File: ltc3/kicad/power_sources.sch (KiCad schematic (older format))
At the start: 8 parts

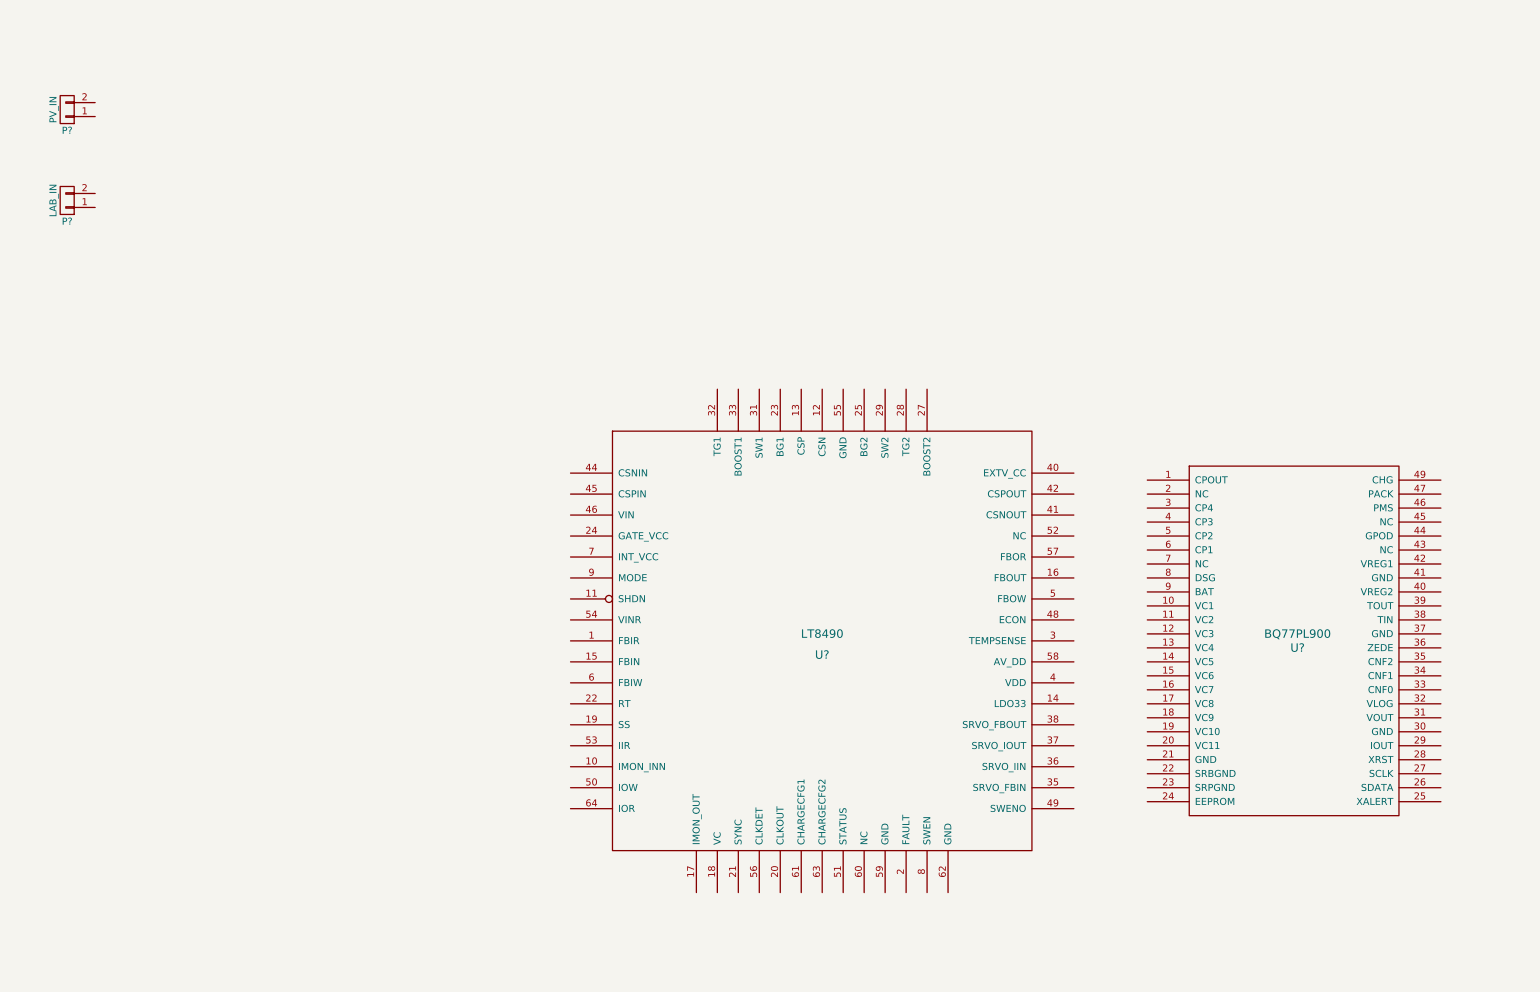
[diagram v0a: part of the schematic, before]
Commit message: Progress on merging master with Charging_Circuit branch.
Still have plenty of schematic clean-up to perform.  There's a lot
going on around the LT8490.
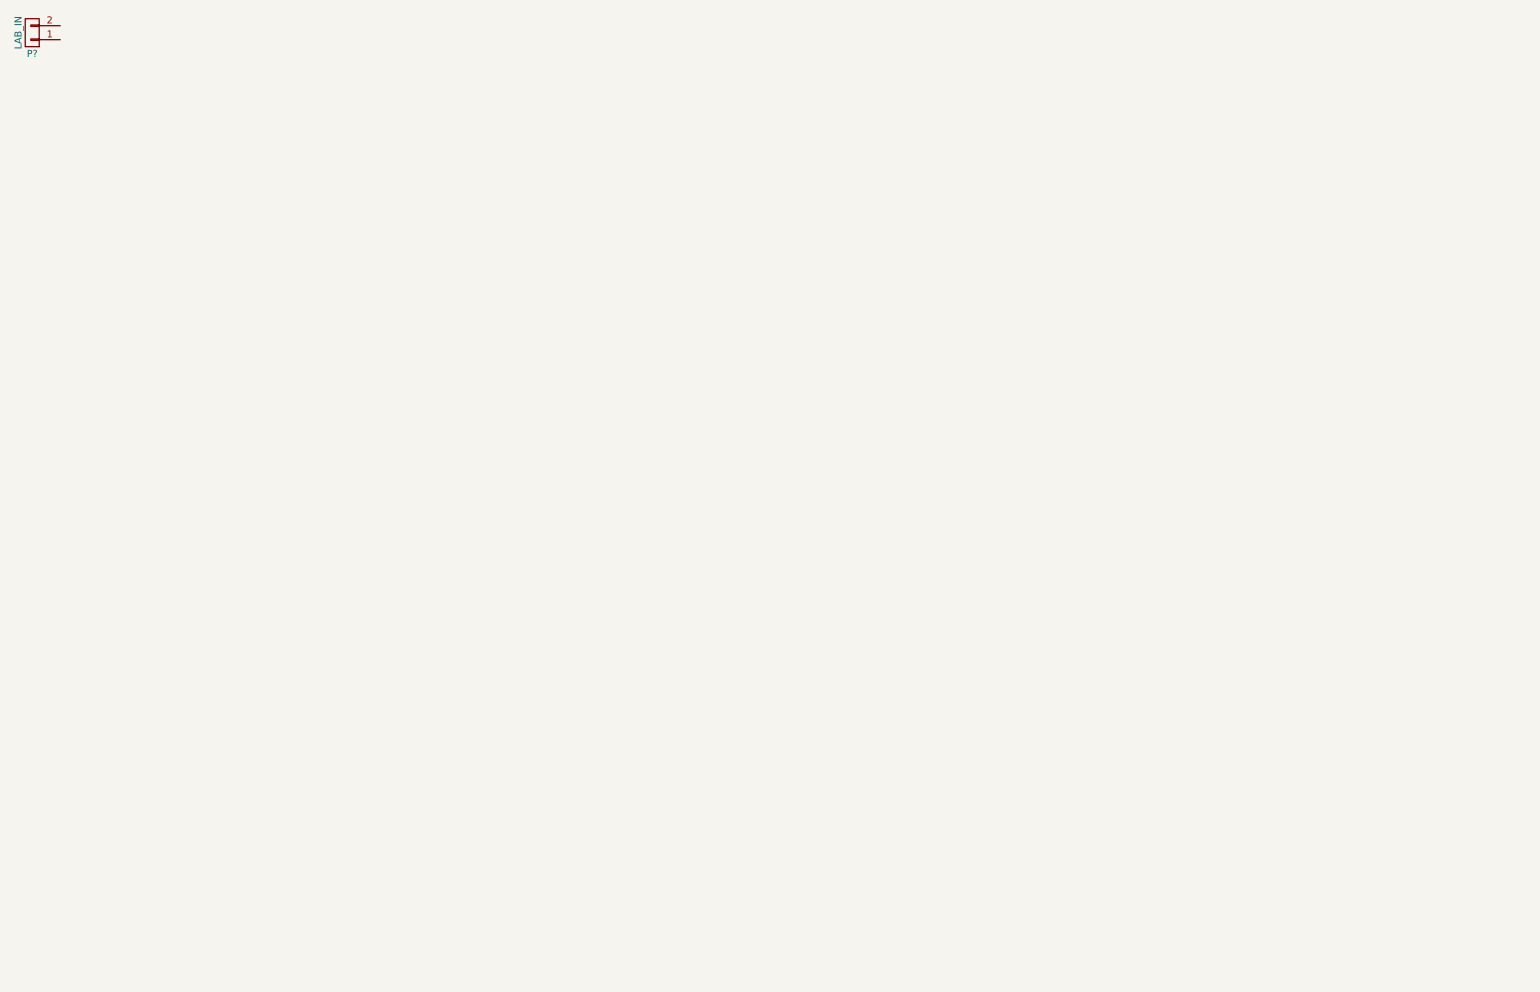
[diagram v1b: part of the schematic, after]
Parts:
- removed P?: PV_IN, symbol CONN_01X02
- removed U?: BQ77PL900, symbol BQ77PL900
- removed U?: LT8490, symbol LT8490
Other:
- moved on the sheet: P?
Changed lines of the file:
@@
-$Comp
-L CONN_01X02 P?
-U 1 1 5583855E
-P 1100 1300
-F 0 "P?" H 1100 1450 50  0000 C CNN
-F 1 "PV_IN" V 1200 1300 50  0000 C CNN
-F 2 "" H 1100 1300 60  0000 C CNN
-F 3 "" H 1100 1300 60  0000 C CNN
-	1    1100 1300
-	-1   0    0    1
-$EndComp
 $Comp
 L CONN_01X02 P?
 U 1 1 55838585
-P 1100 1950
-F 0 "P?" H 1100 2100 50  0000 C CNN
-F 1 "LAB_IN" V 1200 1950 50  0000 C CNN
-F 2 "" H 1100 1950 60  0000 C CNN
-F 3 "" H 1100 1950 60  0000 C CNN
-	1    1100 1950
+P 850 750
+F 0 "P?" H 850 900 50  0000 C CNN
+F 1 "LAB_IN" V 950 750 50  0000 C CNN
+F 2 "" H 850 750 60  0000 C CNN
+F 3 "" H 850 750 60  0000 C CNN
+	1    850  750
 	-1   0    0    1
 $EndComp
@@
 Text Notes 15850 8850 2    60   ~ 0
 Temperature Sensor, Main Battery
-$Comp
-L LT8490 U?
-U 1 1 560CC4C9
-P 6500 5100
-F 0 "U?" H 6500 5000 60  0000 C CNN
-F 1 "LT8490" H 6500 5150 60  0000 C CNN
-F 2 "" H 6550 5200 60  0000 C CNN
-F 3 "" H 6550 5200 60  0000 C CNN
-	1    6500 5100
-	1    0    0    -1
-$EndComp
-$Comp
-L BQ77PL900 U?
-U 1 1 560CC0A7
-P 9900 5100
-F 0 "U?" H 9900 5050 60  0000 C CNN
-F 1 "BQ77PL900" H 9900 5150 60  0000 C CNN
-F 2 "" H 9900 5100 60  0000 C CNN
-F 3 "" H 9900 5100 60  0000 C CNN
-	1    9900 5100
-	1    0    0    -1
-$EndComp
 $EndSCHEMATC

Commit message: Deleted "Power Sources" sheet.
Moved what little circuity it contained into the "Battery Charging"
and "Battery Balancing" sheets.
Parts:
- removed C?: 470p, symbol C
- removed P?: LAB_IN, symbol CONN_01X02
- removed Q?: MMBT3904, symbol Q_NPN_BCE
- removed R? (x2): R, symbol R
- added R?: R4T, symbol R4T
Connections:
- net labels removed: BB_TEMP_BATT+, BB_TEMP_BATT-, BB_VSENSE_PV+, BB_VSENSE_PV-
- wire segments 20 -> 7
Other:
- note removed: "LiPo Batteries"
- note removed: "Temperature Sensor, Main Battery"
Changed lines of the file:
@@
 Text HLabel 15150 2850 2    60   Output ~ 0
 VCC_BATT
-Wire Notes Line
-	14400 5500 15750 5500
-Wire Notes Line
-	15750 5500 15750 6750
-Wire Notes Line
-	15750 6750 14400 6750
-Wire Notes Line
-	14400 6750 14400 5500
-Text Notes 14550 5800 0    100  ~ 0
-LiPo Batteries
-$Comp
-L CONN_01X02 P?
-U 1 1 55838585
-P 850 750
-F 0 "P?" H 850 900 50  0000 C CNN
-F 1 "LAB_IN" V 950 750 50  0000 C CNN
-F 2 "" H 850 750 60  0000 C CNN
-F 3 "" H 850 750 60  0000 C CNN
-	1    850  750
-	-1   0    0    1
-$EndComp
-Connection ~ 14900 3150
-Wire Wire Line
-	15150 3150 14900 3150
-Connection ~ 14400 2850
-Wire Wire Line
-	14400 3000 14400 2850
-Wire Wire Line
-	15150 3000 14400 3000
 Connection ~ 14900 2850
 Wire Wire Line
@@
 Wire Wire Line
 	14800 2850 15150 2850
+Wire Wire Line
+	14150 2850 14500 2850
+Text HLabel 15150 3150 2    60   Output ~ 0
+BB_VSENSE_BATT-
+Text HLabel 15150 3050 2    60   Output ~ 0
+BB_VSENSE_BATT+
+Text Notes 14500 4700 0    100  ~ 0
+R_sense = 1/Imax**2\n1 A = 1 ohm\n3 A = 0.1 ohm\n5 A = 0.04 ohms\n10 A = 0.01 ohms
 $Comp
-L R R?
-U 1 1 55BE1E65
+L R4T R?
+U 1 1 56357239
 P 14650 2850
-F 0 "R?" V 14730 2850 50  0000 C CNN
-F 1 "R" V 14650 2850 50  0000 C CNN
+F 0 "R?" V 14600 2700 50  0000 C CNN
+F 1 "R4T" V 14650 2850 50  0000 C CNN
 F 2 "" V 14580 2850 30  0000 C CNN
 F 3 "" H 14650 2850 30  0000 C CNN
-F 4 "1W, 1%" V 14550 2850 60  0000 C CNN "Note"
+F 4 "1W 1%" V 14550 2950 60  0000 C CNN "Note"
 	1    14650 2850
 	0    1    1    0
 $EndComp
 Wire Wire Line
-	14150 2850 14500 2850
-Text HLabel 15150 3150 2    60   Output ~ 0
-BB_VSENSE_BATT-
-Text HLabel 15150 3000 2    60   Output ~ 0
-BB_VSENSE_BATT+
-Connection ~ 14900 2050
+	15150 3050 14600 3050
 Wire Wire Line
-	15150 2050 14900 2050
-Connection ~ 14400 1750
+	14600 3050 14600 2950
 Wire Wire Line
-	14400 1900 14400 1750
+	15150 3150 14700 3150
 Wire Wire Line
-	15150 1900 14400 1900
-Connection ~ 14900 1750
-Wire Wire Line
-	14900 1750 14900 2300
-Wire Wire Line
-	14800 1750 15150 1750
-$Comp
-L R R?
-U 1 1 55BE4A9F
-P 14650 1750
-F 0 "R?" V 14730 1750 50  0000 C CNN
-F 1 "R" V 14650 1750 50  0000 C CNN
-F 2 "" V 14580 1750 30  0000 C CNN
-F 3 "" H 14650 1750 30  0000 C CNN
-F 4 "1W, 1%" V 14550 1750 60  0000 C CNN "Note"
-	1    14650 1750
-	0    1    1    0
-$EndComp
-Wire Wire Line
-	14150 1750 14500 1750
-Text HLabel 15150 2050 2    60   Output ~ 0
-BB_VSENSE_PV-
-Text HLabel 15150 1900 2    60   Output ~ 0
-BB_VSENSE_PV+
-Text Notes 14500 4700 0    100  ~ 0
-R_sense = 1/Imax**2\n1 A = 1 ohm\n3 A = 0.1 ohm\n5 A = 0.04 ohms\n10 A = 0.01 ohms
-$Comp
-L Q_NPN_BCE Q?
-U 1 1 55C1857A
-P 15250 8050
-F 0 "Q?" H 15550 8100 50  0000 R CNN
-F 1 "MMBT3904" H 15850 8000 50  0000 R CNN
-F 2 "" H 15450 8150 29  0000 C CNN
-F 3 "" H 15250 8050 60  0000 C CNN
-	1    15250 8050
-	1    0    0    -1
-$EndComp
-$Comp
-L C C?
-U 1 1 55C1A85C
-P 14900 8350
-F 0 "C?" H 14925 8450 50  0000 L CNN
-F 1 "470p" H 14925 8250 50  0000 L CNN
-F 2 "" H 14938 8200 30  0000 C CNN
-F 3 "" H 14900 8350 60  0000 C CNN
-	1    14900 8350
-	1    0    0    -1
-$EndComp
-Wire Wire Line
-	14900 7700 14900 8200
-Wire Wire Line
-	14750 8050 15050 8050
-Wire Wire Line
-	14900 7700 15350 7700
-Wire Wire Line
-	15350 7700 15350 7850
-Connection ~ 14900 8050
-Wire Wire Line
-	15350 8250 15350 8650
-Wire Wire Line
-	15350 8650 14900 8650
-Wire Wire Line
-	14900 8650 14900 8500
-Text HLabel 14750 8050 0    60   Output ~ 0
-BB_TEMP_BATT+
-Wire Wire Line
-	15500 8400 15350 8400
-Connection ~ 15350 8400
-Text HLabel 15500 8400 2    60   Output ~ 0
-BB_TEMP_BATT-
-Text Notes 15850 8850 2    60   ~ 0
-Temperature Sensor, Main Battery
+	14700 3150 14700 2950
 $EndSCHEMATC
